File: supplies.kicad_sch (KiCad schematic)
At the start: 33 parts, among them J10 Conn_XT_Sink, U18 LMR36520, U19 LMR36520, U20 LM7812_TO220, U25 tps3824-50

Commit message: tweaks
round size
add some new pads
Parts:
- added s42: 12V, invendelirium_general:pad_1.2x1.5, symbol Connector:TestPoint
- added s43: 5V, invendelirium_general:pad_1.2x1.5, symbol Connector:TestPoint
- added s44: 15V, invendelirium_general:pad_1.2x1.5, symbol Connector:TestPoint
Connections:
- net 12V: now also s42.1
- net 15V: now also s44.1
- net 5V: now also s43.1

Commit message: fill in some part numbers
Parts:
- L9: PN (none) -> SPM6545VT-330M-D
- s25, s42, s43, s44: now left out of the parts list
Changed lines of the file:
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@@
 		(unit 1)
 		(exclude_from_sim no)
-		(in_bom yes)
+		(in_bom no)
 		(on_board yes)
 		(dnp no)
@@
 		(unit 1)
 		(exclude_from_sim no)
-		(in_bom yes)
+		(in_bom no)
 		(on_board yes)
 		(dnp no)
@@
 			)
 		)
+		(property "PN" "SPM6545VT-330M-D"
+			(at 132.08 58.42 0)
+			(effects
+				(font
+					(size 1.27 1.27)
+				)
+				(hide yes)
+			)
+		)
 		(pin "1"
 		)
@@
 		(unit 1)
 		(exclude_from_sim no)
-		(in_bom yes)
+		(in_bom no)
 		(on_board yes)
 		(dnp no)
@@
 		(unit 1)
 		(exclude_from_sim no)
-		(in_bom yes)
+		(in_bom no)
 		(on_board yes)
 		(dnp no)

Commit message: update partnumbers to what was bought
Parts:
- CU18_0: PN GRM21BD72A225ME1K -> GRM21BD72A225ME1L
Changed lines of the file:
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@@
 			)
 		)
-		(property "PN" "GRM21BD72A225ME1K"
+		(property "PN" "GRM21BD72A225ME1L"
 			(at 72.39 60.96 90)
 			(effects

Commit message: update values to what's being used + mark thin film resistors
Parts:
- R187: value 7.5k -> 13k
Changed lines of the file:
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@@
 			)
 		)
-		(property "Value" "7.5k"
+		(property "Value" "13k"
 			(at 140.97 109.855 0)
 			(effects

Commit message: work on bugs...
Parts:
- added R10: 0.3, invendelirium_audio:R_0603, symbol Device:R_Small
- R181, R188: value 3.3k -> 3k
- R182: value 47k -> 36k
- R187: value 13k -> 12k
- U20: value LM7812_TO220 -> LM2940CT-12; PN L7812CV -> LM2940CT-12/NOPB
- s44: value 15V -> 13V
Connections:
- net 12V: now also R10.1; no longer U20.3 (VO)
- new net: R10.2, U20.3 (VO)
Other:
- note added: "13V"
- moved on the sheet: C131, CU20, s42

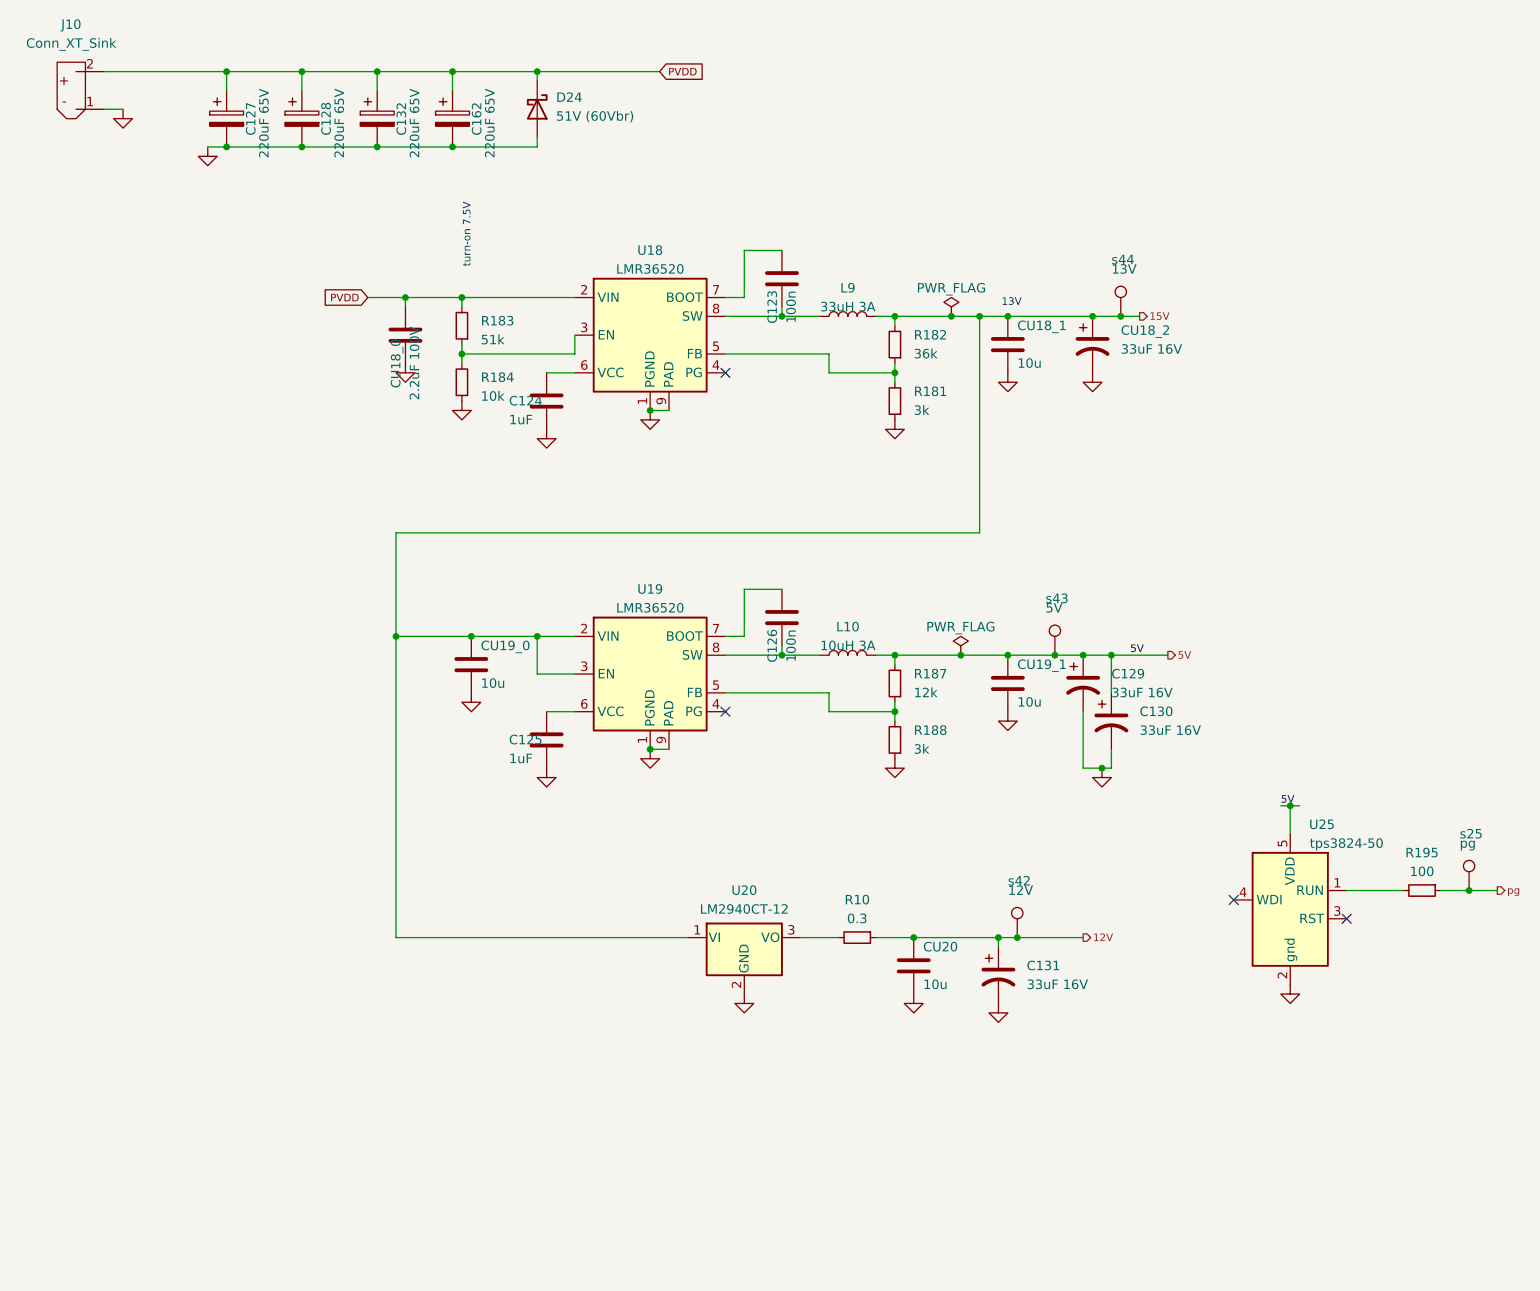
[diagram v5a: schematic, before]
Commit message: work on bugs
* align parts
* enlarge cercaps
* fix ak caps
* improve jack footprint
* fix lmr stencil openings
* remove one ldo
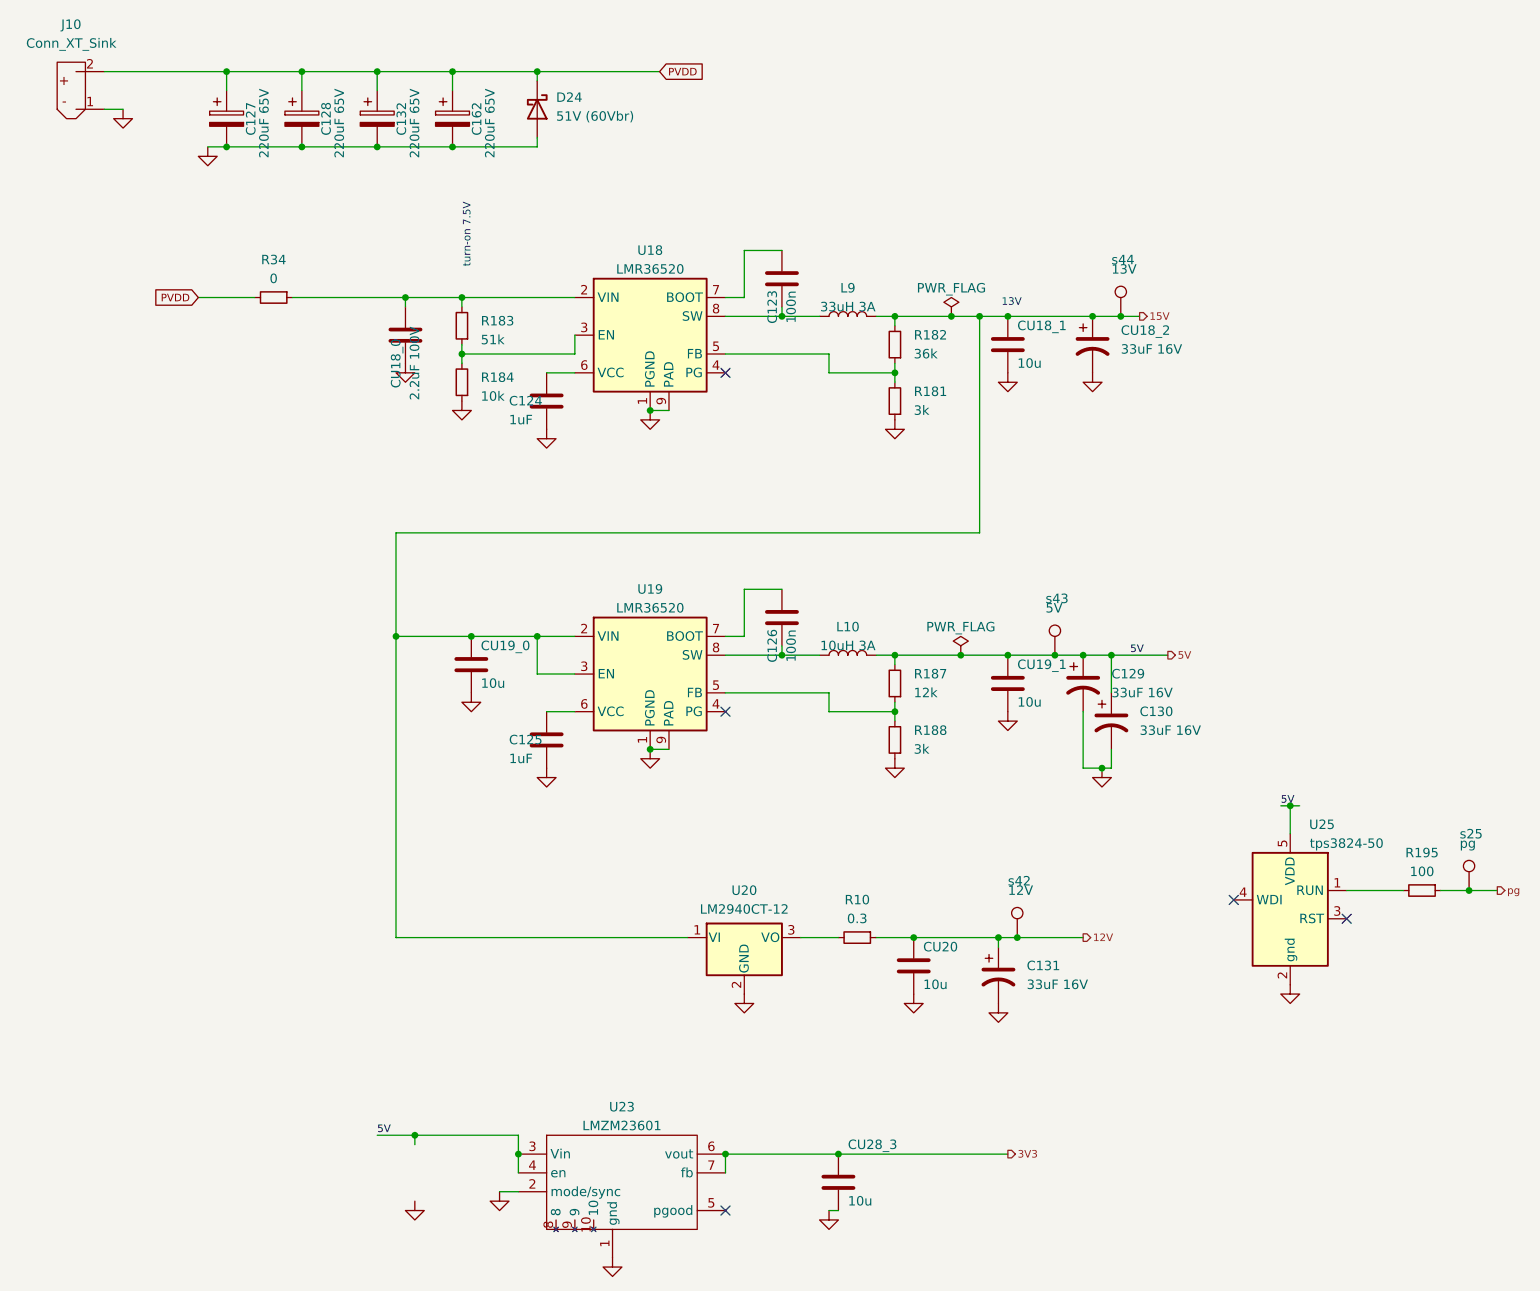
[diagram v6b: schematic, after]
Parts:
- added CU28_3: 10u, invendelirium_audio:C_0603_larger, symbol Device:C
- added R34: 0, invendelirium_audio:R_0603, symbol Device:R_Small
- added U23: LMZM23601, invendelirium_general:LMZM23601, symbol invendelirium_ic:LMZM23601
- CU18_1, CU19_0, CU19_1, CU20: footprint invendelirium_audio:C_0603 -> invendelirium_audio:C_0603_larger
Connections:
- net 5V: now also U23.3 (Vin), U23.4 (en)
- net GND: now also CU28_3.2, U23.1 (gnd), U23.2 (mode/sync), U23.pad
- net PVDD: now also R34.2; no longer CU18_0.1, R183.2, U18.2 (VIN)
- new net: CU18_0.1, R183.2, R34.1, U18.2 (VIN)
- new net 3V3: CU28_3.1, U23.6 (vout), U23.7 (fb)
- no-connect marks 4 -> 5

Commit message: work on bugs
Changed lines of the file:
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@@
 	)
 	(junction
+		(at 62.23 55.88)
+		(diameter 0)
+		(color 0 0 0 0)
+	)
+	(junction
 		(at 215.9 135.89)
 		(diameter 0)
@@
 	)
 	(junction
-		(at 73.66 168.91)
-		(diameter 0)
-		(color 0 0 0 0)
-	)
-	(junction
 		(at 105.41 71.12)
 		(diameter 0)
@@
 	)
 	(junction
+		(at 148.59 142.24)
+		(diameter 0)
+		(color 0 0 0 0)
+	)
+	(junction
 		(at 78.74 35.56)
 		(diameter 0)
@@
 	(wire
 		(pts
-			(xy 87.63 168.91) (xy 73.66 168.91)
-		)
-		(stroke
-			(width 0)
-			(type default)
-		)
-	)
-	(wire
-		(pts
 			(xy 71.12 142.24) (xy 71.12 101.6)
 		)
@@
 	(wire
 		(pts
+			(xy 148.59 142.24) (xy 152.4 142.24)
+		)
+		(stroke
+			(width 0)
+			(type default)
+		)
+	)
+	(wire
+		(pts
 			(xy 168.91 58.42) (xy 171.45 58.42)
 		)
@@
 	(wire
 		(pts
-			(xy 68.58 168.91) (xy 73.66 168.91)
+			(xy 68.58 168.91) (xy 87.63 168.91)
 		)
 		(stroke
@@
 	(wire
 		(pts
-			(xy 73.66 168.91) (xy 73.66 170.18)
-		)
-		(stroke
-			(width 0)
-			(type default)
-		)
-	)
-	(wire
-		(pts
 			(xy 48.26 35.56) (xy 58.42 35.56)
 		)
@@
 	(wire
 		(pts
-			(xy 57.15 55.88) (xy 72.39 55.88)
+			(xy 57.15 55.88) (xy 62.23 55.88)
 		)
 		(stroke
@@
 	(wire
 		(pts
-			(xy 140.97 142.24) (xy 152.4 142.24)
+			(xy 140.97 142.24) (xy 148.59 142.24)
 		)
 		(stroke
@@
 	(wire
 		(pts
+			(xy 62.23 55.88) (xy 72.39 55.88)
+		)
+		(stroke
+			(width 0)
+			(type default)
+		)
+	)
+	(wire
+		(pts
 			(xy 167.64 104.14) (xy 175.26 104.14)
 		)
@@
 	)
 	(symbol
+		(lib_id "power:PWR_FLAG")
+		(at 62.23 55.88 0)
+		(unit 1)
+		(exclude_from_sim no)
+		(in_bom yes)
+		(on_board yes)
+		(dnp no)
+		(fields_autoplaced yes)
+		(property "Reference" "#FLG02"
+			(at 62.23 53.975 0)
+			(effects
+				(font
+					(size 1.27 1.27)
+				)
+				(hide yes)
+			)
+		)
+		(property "Value" "PWR_FLAG"
+			(at 62.23 52.07 0)
+			(effects
+				(font
+					(size 1.27 1.27)
+				)
+			)
+		)
+		(property "Footprint" ""
+			(at 62.23 55.88 0)
+			(effects
+				(font
+					(size 1.27 1.27)
+				)
+				(hide yes)
+			)
+		)
+		(property "Datasheet" "~"
+			(at 62.23 55.88 0)
+			(effects
+				(font
+					(size 1.27 1.27)
+				)
+				(hide yes)
+			)
+		)
+		(property "Description" ""
+			(at 62.23 55.88 0)
+			(effects
+				(font
+					(size 1.27 1.27)
+				)
+				(hide yes)
+			)
+		)
+		(pin "1"
+		)
+		(instances
+			(project "uberamp1"
+				(path "/310059c1-d84b-43e2-9c9a-0e426c534a12/4d0cf4b6-29af-402d-96b9-0bcbddb66920"
+					(reference "#FLG02")
+					(unit 1)
+				)
+			)
+		)
+	)
+	(symbol
 		(lib_id "power:GND")
 		(at 81.28 109.22 0)
@@
 	)
 	(symbol
+		(lib_id "power:PWR_FLAG")
+		(at 148.59 142.24 0)
+		(unit 1)
+		(exclude_from_sim no)
+		(in_bom yes)
+		(on_board yes)
+		(dnp no)
+		(fields_autoplaced yes)
+		(property "Reference" "#FLG013"
+			(at 148.59 140.335 0)
+			(effects
+				(font
+					(size 1.27 1.27)
+				)
+				(hide yes)
+			)
+		)
+		(property "Value" "PWR_FLAG"
+			(at 148.59 138.43 0)
+			(effects
+				(font
+					(size 1.27 1.27)
+				)
+			)
+		)
+		(property "Footprint" ""
+			(at 148.59 142.24 0)
+			(effects
+				(font
+					(size 1.27 1.27)
+				)
+				(hide yes)
+			)
+		)
+		(property "Datasheet" "~"
+			(at 148.59 142.24 0)
+			(effects
+				(font
+					(size 1.27 1.27)
+				)
+				(hide yes)
+			)
+		)
+		(property "Description" ""
+			(at 148.59 142.24 0)
+			(effects
+				(font
+					(size 1.27 1.27)
+				)
+				(hide yes)
+			)
+		)
+		(pin "1"
+		)
+		(instances
+			(project "uberamp1"
+				(path "/310059c1-d84b-43e2-9c9a-0e426c534a12/4d0cf4b6-29af-402d-96b9-0bcbddb66920"
+					(reference "#FLG013")
+					(unit 1)
+				)
+			)
+		)
+	)
+	(symbol
 		(lib_id "victor_strawlab:Conn_XT_Sink")
 		(at 26.67 27.94 0)
@@
 					(unit 1)
 				)
-			)
-		)
-	)
-	(symbol
-		(lib_id "power:GND")
-		(at 73.66 177.8 0)
-		(unit 1)
-		(exclude_from_sim no)
-		(in_bom yes)
-		(on_board yes)
-		(dnp no)
-		(fields_autoplaced yes)
-		(property "Reference" "#PWR06"
-			(at 73.66 184.15 0)
-			(effects
-				(font
-					(size 1.27 1.27)
-				)
-				(hide yes)
-			)
-		)
-		(property "Value" "GND"
-			(at 73.66 182.88 0)
-			(effects
-				(font
-					(size 1.27 1.27)
-				)
-				(hide yes)
-			)
-		)
-		(property "Footprint" ""
-			(at 73.66 177.8 0)
-			(effects
-				(font
-					(size 1.27 1.27)
-				)
-				(hide yes)
-			)
-		)
-		(property "Datasheet" ""
-			(at 73.66 177.8 0)
-			(effects
-				(font
-					(size 1.27 1.27)
-				)
-				(hide yes)
-			)
-		)
-		(property "Description" ""
-			(at 73.66 177.8 0)
-			(effects
-				(font
-					(size 1.27 1.27)
-				)
-				(hide yes)
-			)
-		)
-		(pin "1"
-		)
-		(instances
-			(project "uberamp1"
-				(path "/310059c1-d84b-43e2-9c9a-0e426c534a12/4d0cf4b6-29af-402d-96b9-0bcbddb66920"
-					(reference "#PWR06")
-					(unit 1)
-				)

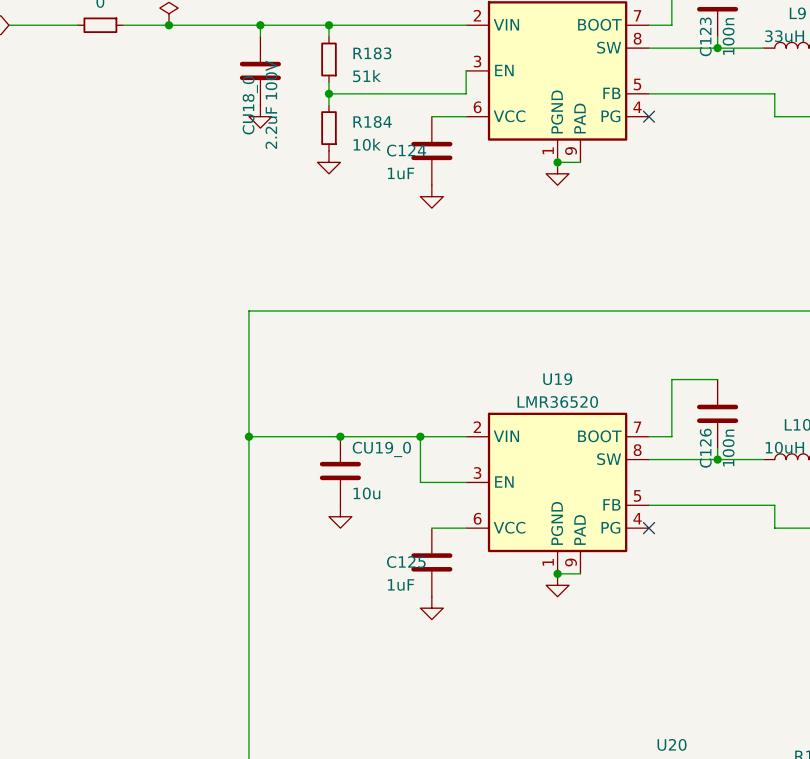
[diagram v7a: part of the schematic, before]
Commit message: updates for better bom
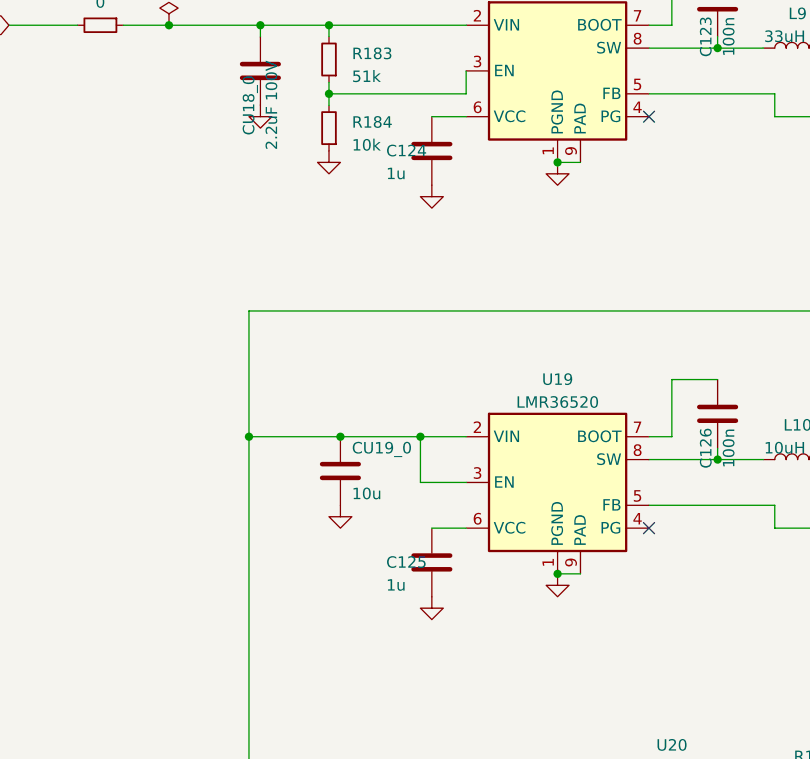
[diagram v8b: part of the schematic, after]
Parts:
- C124, C125: value 1uF -> 1u
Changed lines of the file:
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@@
 			)
 		)
-		(property "Value" "1uF"
+		(property "Value" "1u"
 			(at 86.36 118.11 0)
 			(effects
@@
 			)
 		)
-		(property "Value" "1uF"
+		(property "Value" "1u"
 			(at 86.36 72.39 0)
 			(effects
